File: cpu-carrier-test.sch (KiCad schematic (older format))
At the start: 6 parts, among them SW1 SW_Push

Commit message: hooked up SD-card; use smaller reset button
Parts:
- SW1: footprint Button_Switch_THT:Push_E-Switch_KS01Q01 -> Button_Switch_SMD:SW_SPST_PTS810
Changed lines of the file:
@@
 F 0 "SW1" V 996 1302 50  0000 R CNN
 F 1 "SW_Push" V 905 1302 50  0000 R CNN
-F 2 "Button_Switch_THT:Push_E-Switch_KS01Q01" H 950 1550 50  0001 C CNN
+F 2 "Button_Switch_SMD:SW_SPST_PTS810" H 950 1550 50  0001 C CNN
 F 3 "" H 950 1550 50  0001 C CNN
 	1    950  1350

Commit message: prepare for merge script
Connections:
- net labels added: UART_RX_MIO14, UART_TX_MIO15
- wire segments 73 -> 75
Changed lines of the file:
@@
 $Descr USLetter 11000 8500
 encoding utf-8
-Sheet 1 5
+Sheet 1 6
 Title ""
 Date ""
@@
 Wire Wire Line
 	1550 6650 1650 6650
-$Sheet
-S 4300 1150 1100 1450
-U 5CEAC2F1
-F0 "Power Supply" 50
-F1 "power-and-uart.sch" 50
-$EndSheet
 Text GLabel 8050 4900 0    50   Output ~ 0
 B13_L3_N
@@
 NoConn ~ 2750 5400
 NoConn ~ 2750 5300
+Text GLabel 4400 1500 0    50   Input ~ 0
+UART_TX_MIO15
+Text GLabel 6050 1500 2    50   Output ~ 0
+UART_RX_MIO14
+$Sheet
+S 4600 1100 1150 750
+U 60DAA393
+F0 "power-and-uart" 50
+F1 "power-and-uart/power-test-module.sch" 50
+F2 "UART_TX_OUT" O R 5750 1500 50
+F3 "UART_RX_IN" I L 4600 1500 50
+$EndSheet
+Wire Wire Line
+	6050 1500 5750 1500
+Wire Wire Line
+	4600 1500 4400 1500
 $EndSCHEMATC

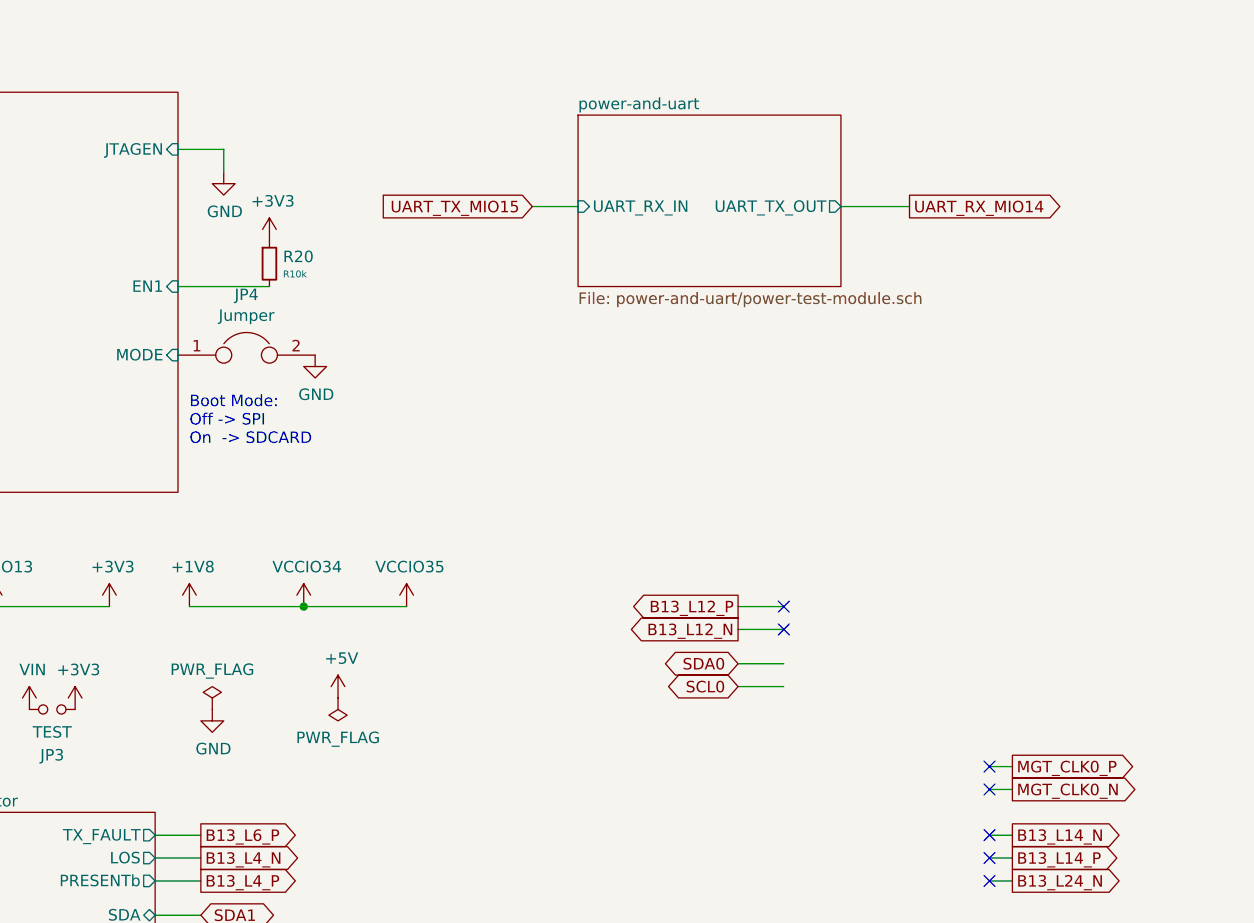
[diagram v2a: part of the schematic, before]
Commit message: final merge of power module; passes DRC
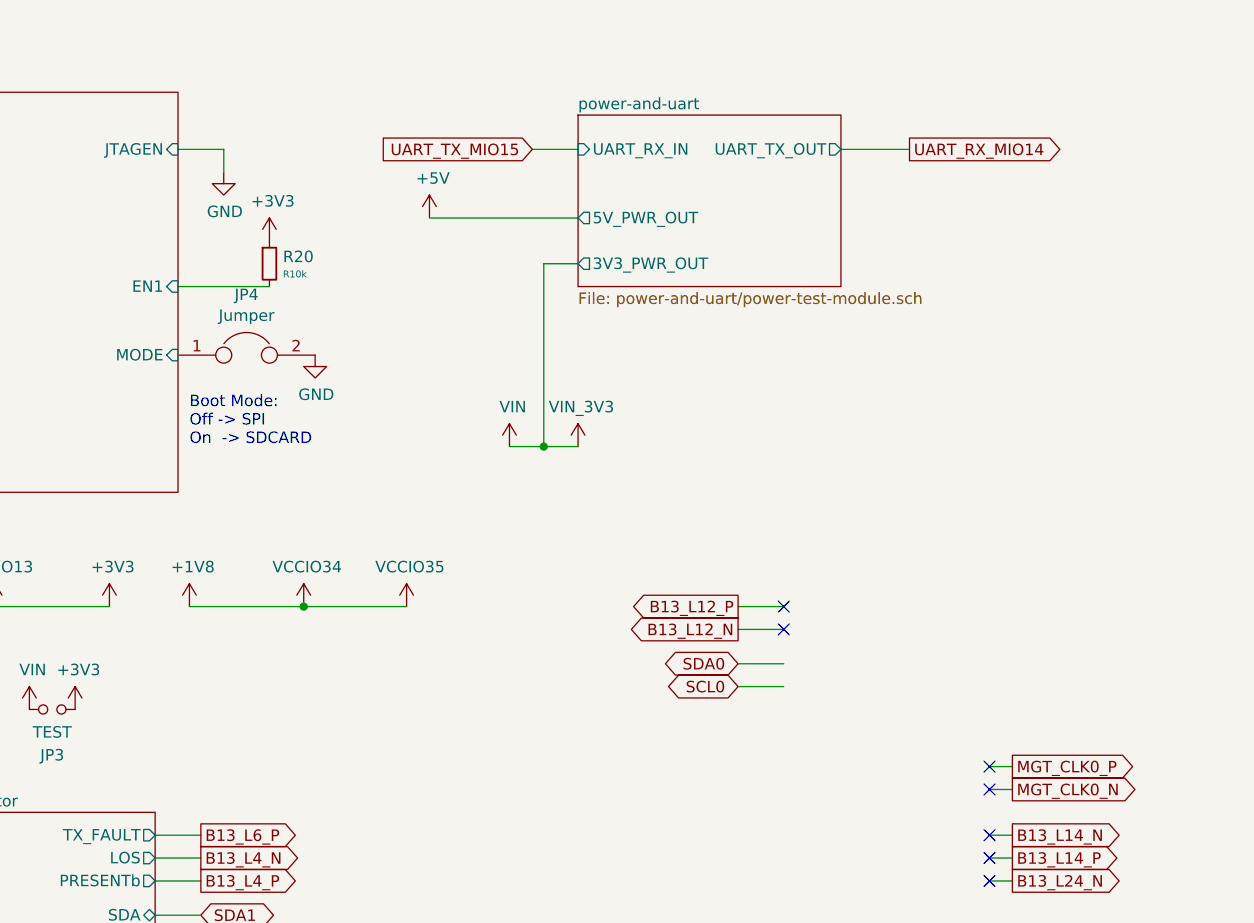
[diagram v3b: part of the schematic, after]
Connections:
- net labels added: VIN_3V3
- wire segments 75 -> 80
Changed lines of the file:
@@
 L power:+5V #PWR?
 U 1 1 5C525614
-P 3550 3650
+P 3950 1550
 AR Path="/5C1147CA/5C525614" Ref="#PWR?"  Part="1"
 AR Path="/5CEAC2F1/5C525614" Ref="#PWR?"  Part="1"
 AR Path="/5C525614" Ref="#PWR?"  Part="1"
-F 0 "#PWR?" H 3550 3500 50  0001 C CNN
-F 1 "+5V" H 3565 3823 50  0000 C CNN
-F 2 "" H 3550 3650 50  0001 C CNN
-F 3 "" H 3550 3650 50  0001 C CNN
-	1    3550 3650
-	1    0    0    -1
-$EndComp
-$Comp
-L power:PWR_FLAG #FLG?
-U 1 1 5C52561A
-P 3550 3650
-AR Path="/5CEAC2F1/5C52561A" Ref="#FLG?"  Part="1"
-AR Path="/5C52561A" Ref="#FLG?"  Part="1"
-F 0 "#FLG?" H 3550 3725 50  0001 C CNN
-F 1 "PWR_FLAG" H 3550 3824 50  0000 C CNN
-F 2 "" H 3550 3650 50  0001 C CNN
-F 3 "~" H 3550 3650 50  0001 C CNN
-	1    3550 3650
-	1    0    0    1
-$EndComp
-$Comp
-L power:GND #PWR?
-U 1 1 5C525620
-P 3000 3700
-AR Path="/5CEAC2F1/5C525620" Ref="#PWR?"  Part="1"
-AR Path="/5C525620" Ref="#PWR?"  Part="1"
-F 0 "#PWR?" H 3000 3450 50  0001 C CNN
-F 1 "GND" H 3005 3527 50  0000 C CNN
-F 2 "" H 3000 3700 50  0001 C CNN
-F 3 "" H 3000 3700 50  0001 C CNN
-	1    3000 3700
-	1    0    0    -1
-$EndComp
-$Comp
-L power:PWR_FLAG #FLG?
-U 1 1 5C525626
-P 3000 3700
-AR Path="/5CEAC2F1/5C525626" Ref="#FLG?"  Part="1"
-AR Path="/5C525626" Ref="#FLG?"  Part="1"
-F 0 "#FLG?" H 3000 3775 50  0001 C CNN
-F 1 "PWR_FLAG" H 3000 3874 50  0000 C CNN
-F 2 "" H 3000 3700 50  0001 C CNN
-F 3 "~" H 3000 3700 50  0001 C CNN
-	1    3000 3700
+F 0 "#PWR?" H 3950 1400 50  0001 C CNN
+F 1 "+5V" H 3965 1723 50  0000 C CNN
+F 2 "" H 3950 1550 50  0001 C CNN
+F 3 "" H 3950 1550 50  0001 C CNN
+	1    3950 1550
 	1    0    0    -1
 $EndComp
@@
 NoConn ~ 2750 5400
 NoConn ~ 2750 5300
-Text GLabel 4400 1500 0    50   Input ~ 0
+Text GLabel 4400 1250 0    50   Input ~ 0
 UART_TX_MIO15
-Text GLabel 6050 1500 2    50   Output ~ 0
+Text GLabel 6050 1250 2    50   Output ~ 0
 UART_RX_MIO14
 $Sheet
@@
 F0 "power-and-uart" 50
 F1 "power-and-uart/power-test-module.sch" 50
-F2 "UART_TX_OUT" O R 5750 1500 50
-F3 "UART_RX_IN" I L 4600 1500 50
+F2 "UART_TX_OUT" O R 5750 1250 50
+F3 "UART_RX_IN" I L 4600 1250 50
+F4 "3V3_PWR_OUT" O L 4600 1750 50
+F5 "5V_PWR_OUT" O L 4600 1550 50
 $EndSheet
 Wire Wire Line
-	6050 1500 5750 1500
+	4600 1250 4400 1250
+$Comp
+L trigbox:VIN #PWR?
+U 1 1 60DB0332
+P 4300 2550
+AR Path="/5CEAC2F1/60DB0332" Ref="#PWR?"  Part="1"
+AR Path="/60DB0332" Ref="#PWR?"  Part="1"
+F 0 "#PWR?" H 4300 2400 50  0001 C CNN
+F 1 "VIN" H 4315 2723 50  0000 C CNN
+F 2 "" H 4300 2550 50  0001 C CNN
+F 3 "" H 4300 2550 50  0001 C CNN
+	1    4300 2550
+	1    0    0    -1
+$EndComp
+$Comp
+L trigbox:VIN_3V3 #PWR?
+U 1 1 60DD3A54
+P 4600 2550
+AR Path="/5BE73D36/60DD3A54" Ref="#PWR?"  Part="1"
+AR Path="/60DD3A54" Ref="#PWR?"  Part="1"
+F 0 "#PWR?" H 4600 2400 50  0001 C CNN
+F 1 "VIN_3V3" H 4615 2723 50  0000 C CNN
+F 2 "" H 4600 2550 50  0001 C CNN
+F 3 "" H 4600 2550 50  0001 C CNN
+	1    4600 2550
+	1    0    0    -1
+$EndComp
 Wire Wire Line
-	4600 1500 4400 1500
+	4300 2550 4450 2550
+Wire Wire Line
+	5750 1250 6050 1250
+Wire Wire Line
+	3950 1550 4600 1550
+Wire Wire Line
+	4600 1750 4450 1750
+Wire Wire Line
+	4450 1750 4450 2550
+Connection ~ 4450 2550
+Wire Wire Line
+	4450 2550 4600 2550
 $EndSCHEMATC

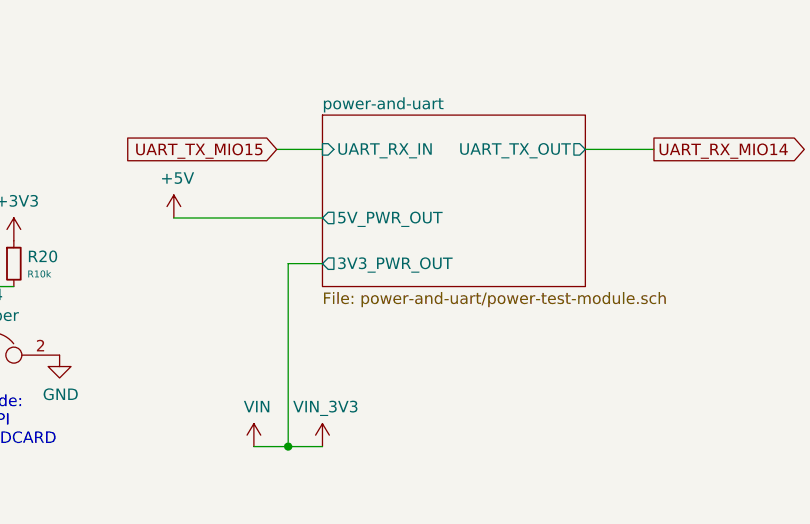
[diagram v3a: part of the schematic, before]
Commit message: integrated power/uart sub-board and fixed design rule violatons
(new violations due to jlcpcb's 0.5mm hole distance)
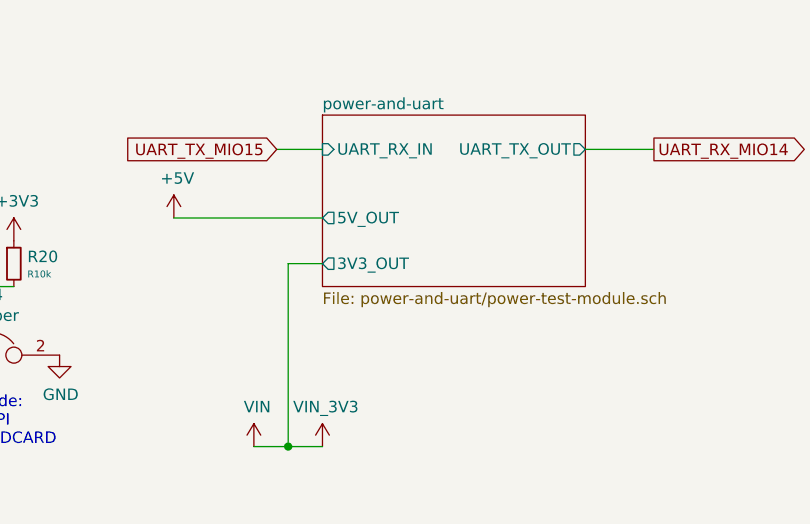
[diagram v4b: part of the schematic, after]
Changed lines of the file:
@@
 Connection ~ 3400 3250
-$Comp
-L power:+5V #PWR?
-U 1 1 5C525614
-P 3950 1550
-AR Path="/5C1147CA/5C525614" Ref="#PWR?"  Part="1"
-AR Path="/5CEAC2F1/5C525614" Ref="#PWR?"  Part="1"
-AR Path="/5C525614" Ref="#PWR?"  Part="1"
-F 0 "#PWR?" H 3950 1400 50  0001 C CNN
-F 1 "+5V" H 3965 1723 50  0000 C CNN
-F 2 "" H 3950 1550 50  0001 C CNN
-F 3 "" H 3950 1550 50  0001 C CNN
-	1    3950 1550
-	1    0    0    -1
-$EndComp
 $Comp
 L Device:Jumper_NO_Small JP?
@@
 NoConn ~ 2750 5400
 NoConn ~ 2750 5300
-Text GLabel 4400 1250 0    50   Input ~ 0
-UART_TX_MIO15
-Text GLabel 6050 1250 2    50   Output ~ 0
-UART_RX_MIO14
-$Sheet
-S 4600 1100 1150 750
-U 60DAA393
-F0 "power-and-uart" 50
-F1 "power-and-uart/power-test-module.sch" 50
-F2 "UART_TX_OUT" O R 5750 1250 50
-F3 "UART_RX_IN" I L 4600 1250 50
-F4 "3V3_PWR_OUT" O L 4600 1750 50
-F5 "5V_PWR_OUT" O L 4600 1550 50
-$EndSheet
 Wire Wire Line
-	4600 1250 4400 1250
+	4450 2550 4600 2550
+Wire Wire Line
+	4450 1750 4450 2550
+Wire Wire Line
+	4600 1750 4450 1750
+Wire Wire Line
+	3950 1550 4600 1550
+Wire Wire Line
+	5750 1250 6050 1250
+Connection ~ 4450 2550
+Wire Wire Line
+	4300 2550 4450 2550
+$Comp
+L trigbox:VIN_3V3 #PWR?
+U 1 1 60DD3A54
+P 4600 2550
+AR Path="/5BE73D36/60DD3A54" Ref="#PWR?"  Part="1"
+AR Path="/60DD3A54" Ref="#PWR?"  Part="1"
+F 0 "#PWR?" H 4600 2400 50  0001 C CNN
+F 1 "VIN_3V3" H 4615 2723 50  0000 C CNN
+F 2 "" H 4600 2550 50  0001 C CNN
+F 3 "" H 4600 2550 50  0001 C CNN
+	1    4600 2550
+	1    0    0    -1
+$EndComp
 $Comp
 L trigbox:VIN #PWR?
@@
 	1    0    0    -1
 $EndComp
+Wire Wire Line
+	4600 1250 4400 1250
+Text GLabel 6050 1250 2    50   Output ~ 0
+UART_RX_MIO14
+Text GLabel 4400 1250 0    50   Input ~ 0
+UART_TX_MIO15
 $Comp
-L trigbox:VIN_3V3 #PWR?
-U 1 1 60DD3A54
-P 4600 2550
-AR Path="/5BE73D36/60DD3A54" Ref="#PWR?"  Part="1"
-AR Path="/60DD3A54" Ref="#PWR?"  Part="1"
-F 0 "#PWR?" H 4600 2400 50  0001 C CNN
-F 1 "VIN_3V3" H 4615 2723 50  0000 C CNN
-F 2 "" H 4600 2550 50  0001 C CNN
-F 3 "" H 4600 2550 50  0001 C CNN
-	1    4600 2550
+L power:+5V #PWR?
+U 1 1 5C525614
+P 3950 1550
+AR Path="/5C1147CA/5C525614" Ref="#PWR?"  Part="1"
+AR Path="/5CEAC2F1/5C525614" Ref="#PWR?"  Part="1"
+AR Path="/5C525614" Ref="#PWR?"  Part="1"
+F 0 "#PWR?" H 3950 1400 50  0001 C CNN
+F 1 "+5V" H 3965 1723 50  0000 C CNN
+F 2 "" H 3950 1550 50  0001 C CNN
+F 3 "" H 3950 1550 50  0001 C CNN
+	1    3950 1550
 	1    0    0    -1
 $EndComp
-Wire Wire Line
-	4300 2550 4450 2550
-Wire Wire Line
-	5750 1250 6050 1250
-Wire Wire Line
-	3950 1550 4600 1550
-Wire Wire Line
-	4600 1750 4450 1750
-Wire Wire Line
-	4450 1750 4450 2550
-Connection ~ 4450 2550
-Wire Wire Line
-	4450 2550 4600 2550
+$Sheet
+S 4600 1100 1150 750
+U 60DAA393
+F0 "power-and-uart" 50
+F1 "power-and-uart/power-test-module.sch" 50
+F2 "3V3_OUT" O L 4600 1750 50
+F3 "5V_OUT" O L 4600 1550 50
+F4 "UART_TX_OUT" O R 5750 1250 50
+F5 "UART_RX_IN" I L 4600 1250 50
+$EndSheet
 $EndSCHEMATC
